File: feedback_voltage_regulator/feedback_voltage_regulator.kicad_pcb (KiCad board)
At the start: 2 copper layers, 135 x 78 mm, 25 parts, among them J1 Power input, J10 Ground point 1, J11 Ground point 2, J12 Input current probe, J13 Ground point 3, J14 Ground point 5, J18 Input current probe, J19 Input current probe, J2 Input current probe, J20 Current short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

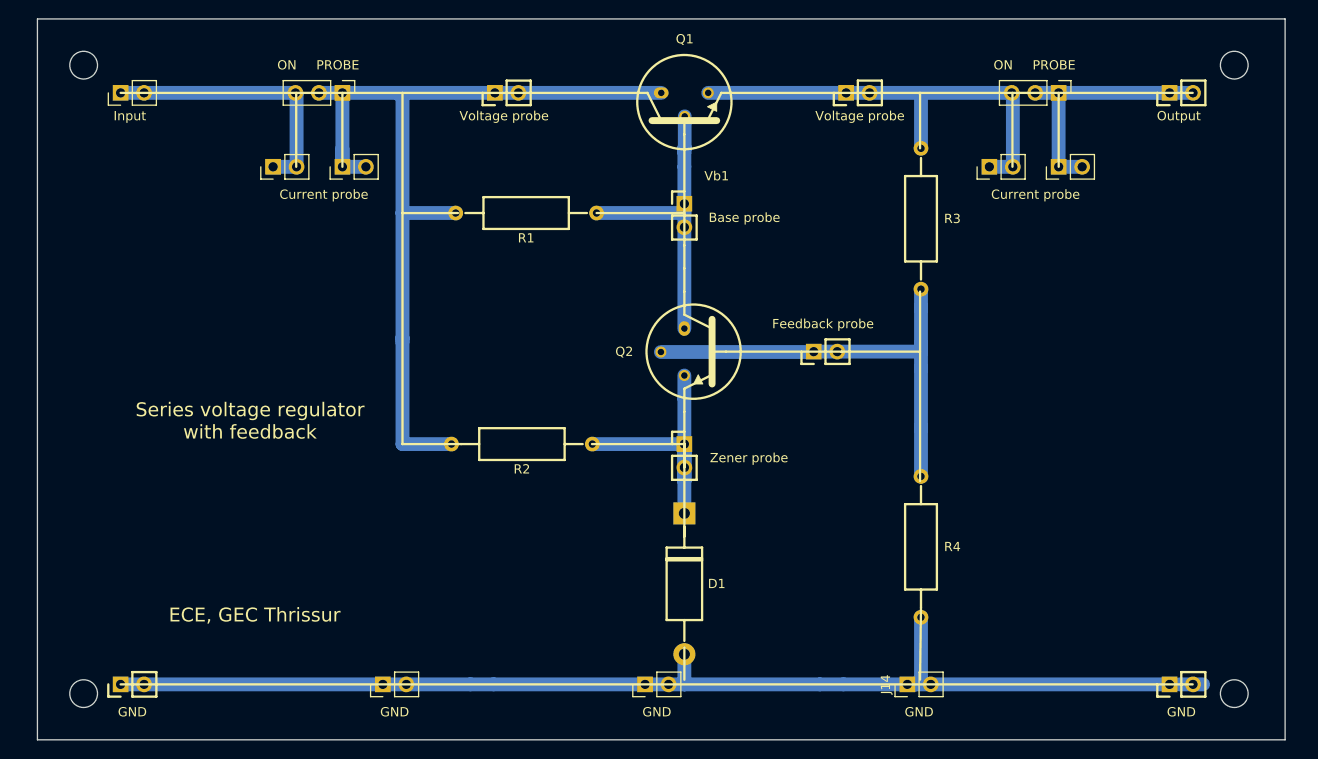
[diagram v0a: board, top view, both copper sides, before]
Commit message: Updated schematic symbols and size
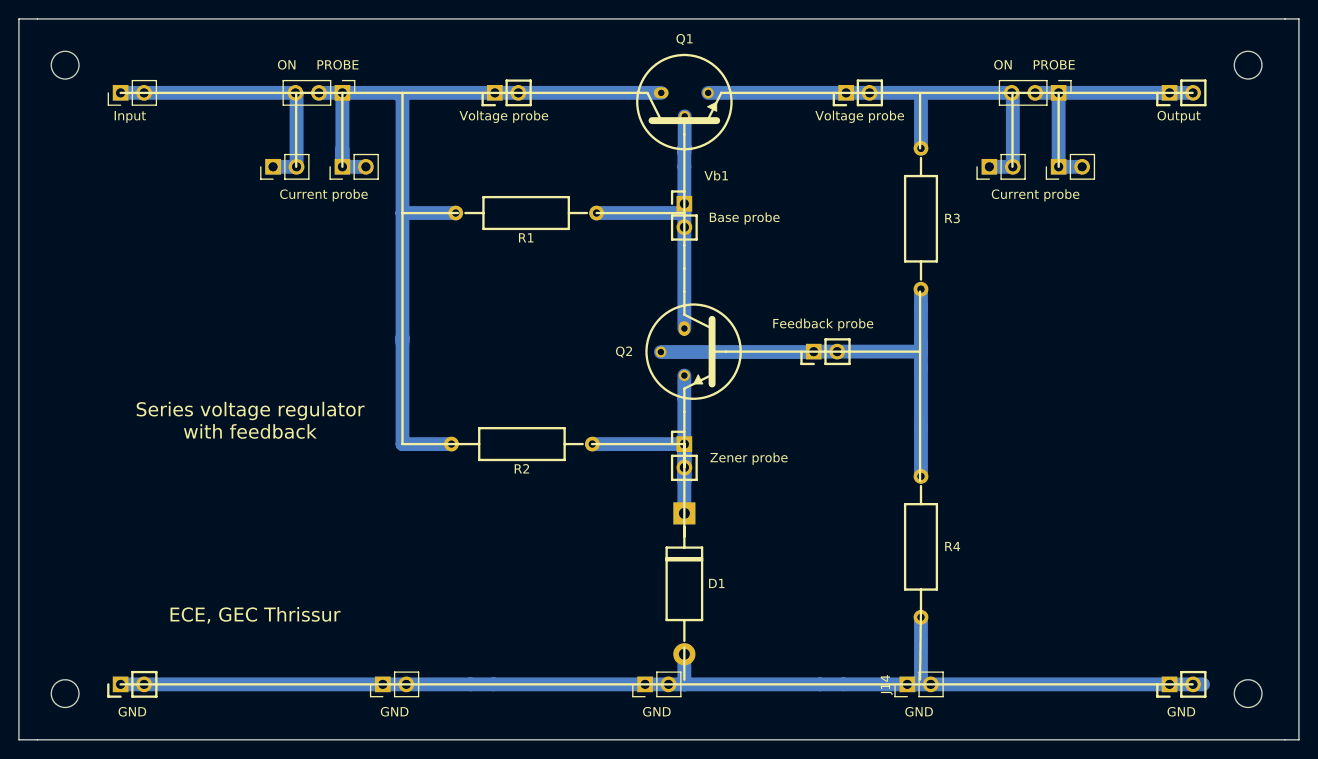
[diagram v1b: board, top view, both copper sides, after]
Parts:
- D1: value D_Zener -> D_Zener_ALT
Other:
- board size 135 x 78 mm -> 138.5 x 78 mm
